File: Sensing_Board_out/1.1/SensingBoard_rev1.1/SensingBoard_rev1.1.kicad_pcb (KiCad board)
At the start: 2 copper layers, 40 x 40 mm, 52 parts, among them J1 USB_C_Receptacle, J2 3221-10-0300-00, J3 F32R-1A7H1-11024, J4 GRPB052VWQP-RC, J5 HMTSW-102-X-X-S-X, J6 HMTSW-102-X-X-S-X, J7 HMTSW-102-X-X-S-X, J8 HMTSW-102-X-X-S-X, SW1 PTS815 SJM 250 SMTR LFS, U1 ESP32C3, U2 BNO055, U3 MIC5504-3.3YM5, U4 FT232RQ

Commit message: finished power board
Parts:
- removed J8: HMTSW-102-X-X-S-X, HMTSW-102-X-X-S-X:SAMTEC_HMTSW-102-X-X-S-X
- added J9: RS1-02-G, RS1-02-G:CONN_RS1-02-G_ADM, F.Cu at (125.3, 41.9)
- J5, J6, J7: value HMTSW-102-X-X-S-X -> RS1-02-G; footprint HMTSW-102-X-X-S-X:SAMTEC_HMTSW-102-X-X-S-X -> RS1-02-G:CONN_RS1-02-G_ADM

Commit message: fixing POE board symbols + circuit
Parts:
- added C14: 1.6pF, Capacitor_SMD:C_0402_1005Metric, F.Cu at (96.5, 41.8)
- added C15: 1.6pF, Capacitor_SMD:C_0402_1005Metric, F.Cu at (96.5, 43.8)
- added C16: 18pF, Capacitor_SMD:C_0201_0603Metric, F.Cu at (99.2, 41.7)
- added C17: 18pF, Capacitor_SMD:C_0201_0603Metric, F.Cu at (99.2, 43.5)
- added C18: 100nF, Capacitor_SMD:C_0402_1005Metric, F.Cu at (96.5, 45.8)
- added C19: 10uF, Capacitor_SMD:C_0603_1608Metric, F.Cu at (107.3, 42.1)
- added C20: 1uF, Capacitor_SMD:C_0201_0603Metric, F.Cu at (99.2, 45.2)
- added C21: 10uF, Capacitor_SMD:C_0603_1608Metric, F.Cu at (107.3, 44.6)
- added C22: 1uF, Capacitor_SMD:C_0201_0603Metric, F.Cu at (99.2, 47.0)
- added C23: 10uF, Capacitor_SMD:C_0603_1608Metric, F.Cu at (107.3, 47.1)
- added C24: 1uF, Capacitor_SMD:C_0201_0603Metric, F.Cu at (101.6, 41.7)
- added C25: 10uF, Capacitor_SMD:C_0603_1608Metric, F.Cu at (107.3, 49.6)
- added C26: 1uF, Capacitor_SMD:C_0201_0603Metric, F.Cu at (101.6, 43.5)
- added C27: 2.2uF, Capacitor_SMD:C_0402_1005Metric, F.Cu at (96.5, 47.7)
- added C28: 2.2uF, Capacitor_SMD:C_0402_1005Metric, F.Cu at (96.5, 49.7)
- added C29: 100nF, Capacitor_SMD:C_0402_1005Metric, F.Cu at (96.5, 51.7)
- added D4: B140-E3, Diode_SMD:D_SMA, F.Cu at (107.9, 36.5)
- added FB1: 120R-3A, Capacitor_SMD:C_0805_2012Metric, F.Cu at (111.5, 51.3)
- added L1: 2nH, Inductor_SMD:L_01005_0402Metric, F.Cu at (113.1, 35.0)
- added L2: 2nH, Inductor_SMD:L_01005_0402Metric, F.Cu at (113.1, 36.7)
- added R21: 10k, Resistor_SMD:R_0201_0603Metric, F.Cu at (101.6, 45.2)
- added R22: 10k, Resistor_SMD:R_0201_0603Metric, F.Cu at (101.6, 47.0)
- added R23: 10k, Resistor_SMD:R_0201_0603Metric, F.Cu at (104.1, 41.7)
- added R24: 10k, Resistor_SMD:R_0201_0603Metric, F.Cu at (104.1, 43.5)
- added R25: 10k, Resistor_SMD:R_0201_0603Metric, F.Cu at (104.1, 45.2)
- added SW2: PTS815 SJM 250 SMTR LFS, PTS815:SW4_PTS815 SJM 250 SMTR LFS_CNK, F.Cu at (100.3, 38.3)
- added U5: MIC5504-1.8YM5, Package_TO_SOT_SMD:SOT-23-5, F.Cu at (111.9, 43.1)
- added U6: MCP1700x-280xxTT, Package_TO_SOT_SMD:SOT-23, F.Cu at (111.7, 47.5)
- added Y1: ABM8G-40.000MHZ-18-D2Y-T, ABM8G_40_000MHZ_18_D2Y_T:CRYSTAL_ABM8G_ABR, F.Cu at (101.8, 50.7)
- moved U4 35.8 mm to (121.4, 70.8)
- moved U1 1.17 mm to (129.0, 70.9)
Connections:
- ANT1 pad GND1: unconnected-(ANT1-PadGND1) -> GND
- ANT1 pad GND2: unconnected-(ANT1-PadGND2) -> GND
- ANT1 pad SIG: unconnected-(ANT1-PadSIG) -> Net-(ANT1-PadSIG)
- C1 pad 1: unconnected-(C1-Pad1) -> GND
- C2 pad 2: unconnected-(C2-Pad2) -> GND
- J3 pad 10: unconnected-(J3-Pad10) -> +1V8
- J3 pad 11: unconnected-(J3-Pad11) -> +2V8
- J3 pad 12: unconnected-(J3-Pad12) -> IO48/DVP_Y9
- J3 pad 13: unconnected-(J3-Pad13) -> IO10/XMCLK
- J3 pad 14: unconnected-(J3-Pad14) -> IO11/DVP_Y8
- J3 pad 15: unconnected-(J3-Pad15) -> GND
- J3 pad 16: unconnected-(J3-Pad16) -> IO12/DVP_Y7
- J3 pad 17: unconnected-(J3-Pad17) -> IO13/DVP_PCLK
- J3 pad 18: unconnected-(J3-Pad18) -> IO14/DVP_Y6
- J3 pad 19: unconnected-(J3-Pad19) -> IO15/DVP_Y2
- J3 pad 2: unconnected-(J3-Pad2) -> GND
- J3 pad 20: unconnected-(J3-Pad20) -> IO16/DVP_Y5
- J3 pad 21: unconnected-(J3-Pad21) -> IO17/DVP_Y3
- J3 pad 22: unconnected-(J3-Pad22) -> IO18/DVP_Y4
- J3 pad 23: unconnected-(J3-Pad23) -> GND
- J3 pad 24: unconnected-(J3-Pad24) -> Net-(D4-K)
- J3 pad 3: unconnected-(J3-Pad3) -> IO40/CAM_SDA
- J3 pad 4: unconnected-(J3-Pad4) -> Net-(FB1-Pad2)
- J3 pad 5: unconnected-(J3-Pad5) -> IO39/CAM_SCL
- J3 pad 6: unconnected-(J3-Pad6) -> CAM_RESET
- J3 pad 7: unconnected-(J3-Pad7) -> IO38/DVP_VSYNC
- J3 pad 8: unconnected-(J3-Pad8) -> Net-(J3-Pad8)
- J3 pad 9: unconnected-(J3-Pad9) -> IO47/DVP_HREF
- SW1 pad 1: unconnected-(SW1-Pad1) -> CHIP_EN
- U1 pad 1: unconnected-(U1-LNA_IN-Pad1) -> Net-(U1-LNA_IN)
- U1 pad 11: unconnected-(U1-VDD3P3_RTC-Pad11) -> VDD3P3_RTC
- U1 pad 17: unconnected-(U1-VDD3P3_CPU-Pad17) -> +3.3V
- U1 pad 18: unconnected-(U1-VDD_SPI-Pad18) -> VDD_SPI
- U1 pad 19: unconnected-(U1-SPIHD-Pad19) -> SPIHD
- U1 pad 2: +3.3V -> Net-(C18-Pad1)
- U1 pad 20: unconnected-(U1-SPIWP-Pad20) -> SPIWP
- U1 pad 21: unconnected-(U1-SPICS0-Pad21) -> SPICS0
- U1 pad 22: unconnected-(U1-SPICLK-Pad22) -> SPICLK
- U1 pad 23: unconnected-(U1-SPID-Pad23) -> SPID
- U1 pad 24: unconnected-(U1-SPIQ-Pad24) -> SPIQ
- U1 pad 29: unconnected-(U1-XTAL_N-Pad29) -> Net-(U1-XTAL_N)
- U1 pad 3: +3.3V -> Net-(C18-Pad1)
- U1 pad 30: unconnected-(U1-XTAL_P-Pad30) -> Net-(U1-XTAL_P)
- U1 pad 31: Net-(U1-VDDA-Pad31) -> +3.3V
- U1 pad 32: Net-(U1-VDDA-Pad31) -> +3.3V
- U1 pad 7: unconnected-(U1-CHIP_EN-Pad7) -> CHIP_EN

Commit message: sense board
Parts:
- added U7: ESP32-S3, ESP32S3:QFN56_7X7_EXP, F.Cu at (93.1, 65.0)

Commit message: completed sense board
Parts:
- removed C4: 22pF, Capacitor_SMD:C_0201_0603Metric
- removed D1: LED, LED_SMD:LED_0603_1608Metric
- removed J4: GRPB052VWQP-RC, GRPB052VWQP-RC:GRPB052VWQPRC
- removed R2: 100, Resistor_SMD:R_0201_0603Metric
- removed U1: ESP32C3, ESP32C3:QFN32_5X5MM
- removed XTAL1: ABS07-32.768KHZ-7-T, ABS07-32.768KHZ-7-T:XTAL_ABS07-32.768KHZ-7-T_ABR
- added C30: 100nF, Capacitor_SMD:C_0402_1005Metric, F.Cu at (166.9, 43.8)
- added C31: 2.2uF, Capacitor_SMD:C_0402_1005Metric, F.Cu at (166.9, 45.7)
- added C32: 2.2uF, Capacitor_SMD:C_0402_1005Metric, F.Cu at (166.9, 47.7)
- added C33: 2.2uF, Capacitor_SMD:C_0402_1005Metric, F.Cu at (166.9, 49.7)
- added C34: 100nF, Capacitor_SMD:C_0402_1005Metric, F.Cu at (166.9, 51.6)
- added C35: 10nF, Capacitor_SMD:C_0402_1005Metric, F.Cu at (166.9, 53.6)
- added C36: 100nF, Capacitor_SMD:C_0402_1005Metric, F.Cu at (166.9, 55.6)
- added C37: 100nF, Capacitor_SMD:C_0402_1005Metric, F.Cu at (166.9, 57.6)
- added R26: 499, Resistor_SMD:R_0201_0603Metric, F.Cu at (169.5, 43.7)
- added R27: 0k, Resistor_SMD:R_0201_0603Metric, F.Cu at (169.5, 45.4)
- added R28: 4.7k, Resistor_SMD:R_0201_0603Metric, F.Cu at (169.5, 47.2)
- C1: value 10uF -> 100nF; footprint Capacitor_SMD:C_0603_1608Metric -> Capacitor_SMD:C_0402_1005Metric
- C2: value 1uF -> 100nF; footprint Capacitor_SMD:C_0201_0603Metric -> Capacitor_SMD:C_0402_1005Metric
- C3: value 22pF -> 4.7uF; footprint Capacitor_SMD:C_0201_0603Metric -> Capacitor_SMD:C_0402_1005Metric
- R22: value 10k -> 0k
- R23: value 10k -> 4.7k
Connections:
- C1 pad 1: GND -> CAM_RESET
- C1 pad 2: +3.3V -> GND
- C14 pad 1: Net-(U1-LNA_IN) -> Net-(U7-LNA_IN)
- C16 pad 1: Net-(U1-XTAL_P) -> Net-(U7-XTAL_P)
- C17 pad 1: Net-(U1-XTAL_N) -> Net-(U7-XTAL_N)
- C3 pad 1: Net-(U1-XTAL_32K_P) -> +3.3V
- D2 pad 1: unconnected-(D2-K-Pad1) -> IO21/USER_LED
- D2 pad 2: unconnected-(D2-A-Pad2) -> Net-(D2-A)
- J3 pad 3: IO40/CAM_SDA -> MTDO/IO40/CAM_SDA
- J3 pad 5: IO39/CAM_SCL -> MTCK/IO39/CAM_SCL
- L1 pad 1: Net-(U1-LNA_IN) -> Net-(U7-LNA_IN)
- R1 pad 1: unconnected-(R1-Pad1) -> Net-(D2-A)
- R1 pad 2: unconnected-(R1-Pad2) -> +3.3V
- R10 pad 2: unconnected-(R10-Pad2) -> D3/A3
- R14 pad 2: unconnected-(R14-Pad2) -> GPIO35
- R15 pad 2: unconnected-(R15-Pad2) -> D2/A2
- R16 pad 2: unconnected-(R16-Pad2) -> D1/A1
- R17 pad 2: unconnected-(R17-Pad2) -> D0/A0
- R18 pad 2: unconnected-(R18-Pad2) -> GPIO37
- R19 pad 2: unconnected-(R19-Pad2) -> GPIO34
- R20 pad 2: unconnected-(R20-Pad2) -> GPIO33
- R22 pad 1: +2V8 -> Net-(R22-Pad1)
- R22 pad 2: IO40/CAM_SDA -> +2V8
- R23 pad 1: +2V8 -> Net-(R22-Pad1)
- R23 pad 2: IO39/CAM_SCL -> MTDO/IO40/CAM_SDA
- R9 pad 2: unconnected-(R9-Pad2) -> GPIO36
- SW2 pad 1: D9 -> GPIO0
- U7 pad 1: unconnected-(U7-LNA_IN-Pad1) -> Net-(U7-LNA_IN)
- U7 pad 10: unconnected-(U7-GPIO5-Pad10) -> D4/I2C_SDA
- U7 pad 11: unconnected-(U7-GPIO6-Pad11) -> D5/I2C_SCL
- U7 pad 12: unconnected-(U7-GPIO7-Pad12) -> D8/A8/SCK
- U7 pad 13: unconnected-(U7-GPIO8-Pad13) -> D9/A9/MISO
- U7 pad 14: unconnected-(U7-GPIO9-Pad14) -> D10/A10/MOSI
- U7 pad 15: unconnected-(U7-GPIO10-Pad15) -> IO10/XMCLK
- U7 pad 16: unconnected-(U7-GPIO11-Pad16) -> IO11/DVP_Y8
- U7 pad 17: unconnected-(U7-GPIO12-Pad17) -> IO12/DVP_Y7
- U7 pad 18: unconnected-(U7-GPIO13-Pad18) -> IO13/DVP_PCLK
- U7 pad 19: unconnected-(U7-GPIO14-Pad19) -> IO14/DVP_Y6
- U7 pad 2: unconnected-(U7-VDD3P3-Pad2) -> Net-(C18-Pad1)
- U7 pad 20: unconnected-(U7-VDD3P3_RTC-Pad20) -> +3.3V
- U7 pad 21: unconnected-(U7-XTAL_32K_P-Pad21) -> IO15/DVP_Y2
- U7 pad 22: unconnected-(U7-XTAL_32K_N-Pad22) -> IO16/DVP_Y5
- U7 pad 23: unconnected-(U7-GPIO17-Pad23) -> IO17/DVP_Y3
- U7 pad 24: unconnected-(U7-GPIO18-Pad24) -> IO18/DVP_Y4
- U7 pad 25: unconnected-(U7-GPIO19-Pad25) -> USB_DN
- U7 pad 26: unconnected-(U7-GPIO20-Pad26) -> USB_DP
- U7 pad 27: unconnected-(U7-GPIO21-Pad27) -> IO21/USER_LED
- U7 pad 29: unconnected-(U7-VDD_SPI-Pad29) -> VDD_SPI
- U7 pad 3: unconnected-(U7-VDD3P3-Pad3) -> Net-(C18-Pad1)
- U7 pad 30: unconnected-(U7-SPIHD-Pad30) -> SPIHD
- U7 pad 31: unconnected-(U7-SPIWP-Pad31) -> SPIWP
- U7 pad 32: unconnected-(U7-SPICS0-Pad32) -> SPICS0
- U7 pad 33: unconnected-(U7-SPICLK-Pad33) -> SPICLK
- U7 pad 34: unconnected-(U7-SPIQ-Pad34) -> SPIQ
- U7 pad 35: unconnected-(U7-SPID-Pad35) -> SPID
- U7 pad 36: unconnected-(U7-SPICLK_N-Pad36) -> IO48/DVP_Y9
- U7 pad 37: unconnected-(U7-SPICLK_P-Pad37) -> IO47/DVP_HREF
- U7 pad 38: unconnected-(U7-GPIO33-Pad38) -> GPIO33
- U7 pad 39: unconnected-(U7-GPIO34-Pad39) -> GPIO34
- U7 pad 4: unconnected-(U7-CHIP_PU-Pad4) -> CHIP_EN
- U7 pad 40: unconnected-(U7-GPIO35-Pad40) -> GPIO35
- U7 pad 41: unconnected-(U7-GPIO36-Pad41) -> GPIO36
- U7 pad 42: unconnected-(U7-GPIO37-Pad42) -> GPIO37
- U7 pad 43: unconnected-(U7-GPIO38-Pad43) -> IO38/DVP_VSYNC
- U7 pad 44: unconnected-(U7-MTCK-Pad44) -> MTCK/IO39/CAM_SCL
- U7 pad 45: unconnected-(U7-MTDO-Pad45) -> MTDO/IO40/CAM_SDA
- U7 pad 46: unconnected-(U7-VDD3P3_CPU-Pad46) -> +3.3V
- U7 pad 47: unconnected-(U7-MTDI-Pad47) -> MTDI/IO41/PDM_DATA
- U7 pad 48: unconnected-(U7-MTMS-Pad48) -> MTMS/IO42/PDM_CLK
- U7 pad 49: unconnected-(U7-U0TXD-Pad49) -> Net-(U7-U0TXD)
- U7 pad 5: unconnected-(U7-GPIO0-Pad5) -> GPIO0
- U7 pad 50: unconnected-(U7-U0RXD-Pad50) -> RX_D7
- U7 pad 53: unconnected-(U7-XTAL_N-Pad53) -> Net-(U7-XTAL_N)
- U7 pad 54: unconnected-(U7-XTAL_P-Pad54) -> Net-(U7-XTAL_P)
- U7 pad 55: unconnected-(U7-VDDA-Pad55) -> +3.3V
- U7 pad 56: unconnected-(U7-VDDA-Pad56) -> +3.3V
- U7 pad 57: unconnected-(U7-GND-Pad57) -> GND
- U7 pad 6: unconnected-(U7-GPIO1-Pad6) -> D0/A0
- U7 pad 7: unconnected-(U7-GPIO2-Pad7) -> D1/A1
- U7 pad 8: unconnected-(U7-GPIO3-Pad8) -> D2/A2
- U7 pad 9: unconnected-(U7-GPIO4-Pad9) -> D3/A3
- Y1 pad 1: Net-(U1-XTAL_N) -> Net-(U7-XTAL_N)
- Y1 pad 3: Net-(U1-XTAL_P) -> Net-(U7-XTAL_P)

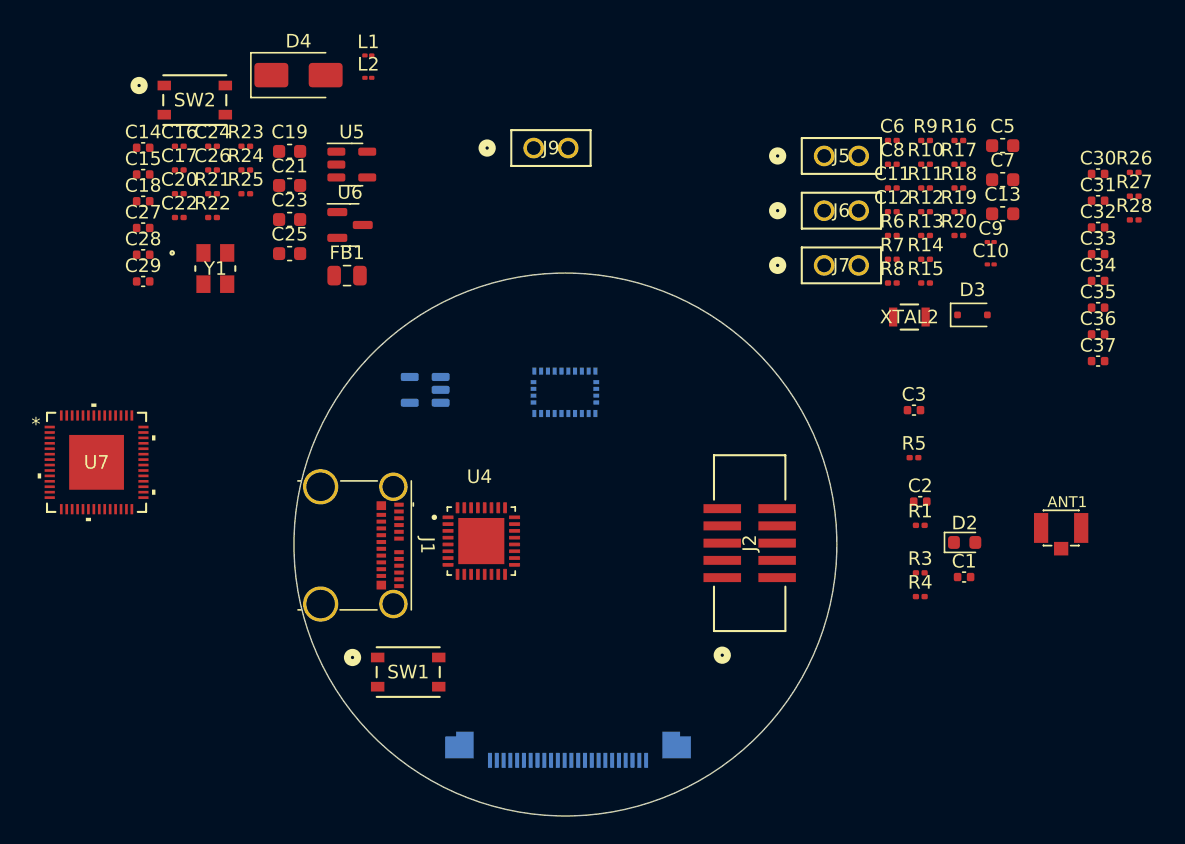
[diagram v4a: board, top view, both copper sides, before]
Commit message: updated power
finished swapping power board bulk cap, new POE board schematic
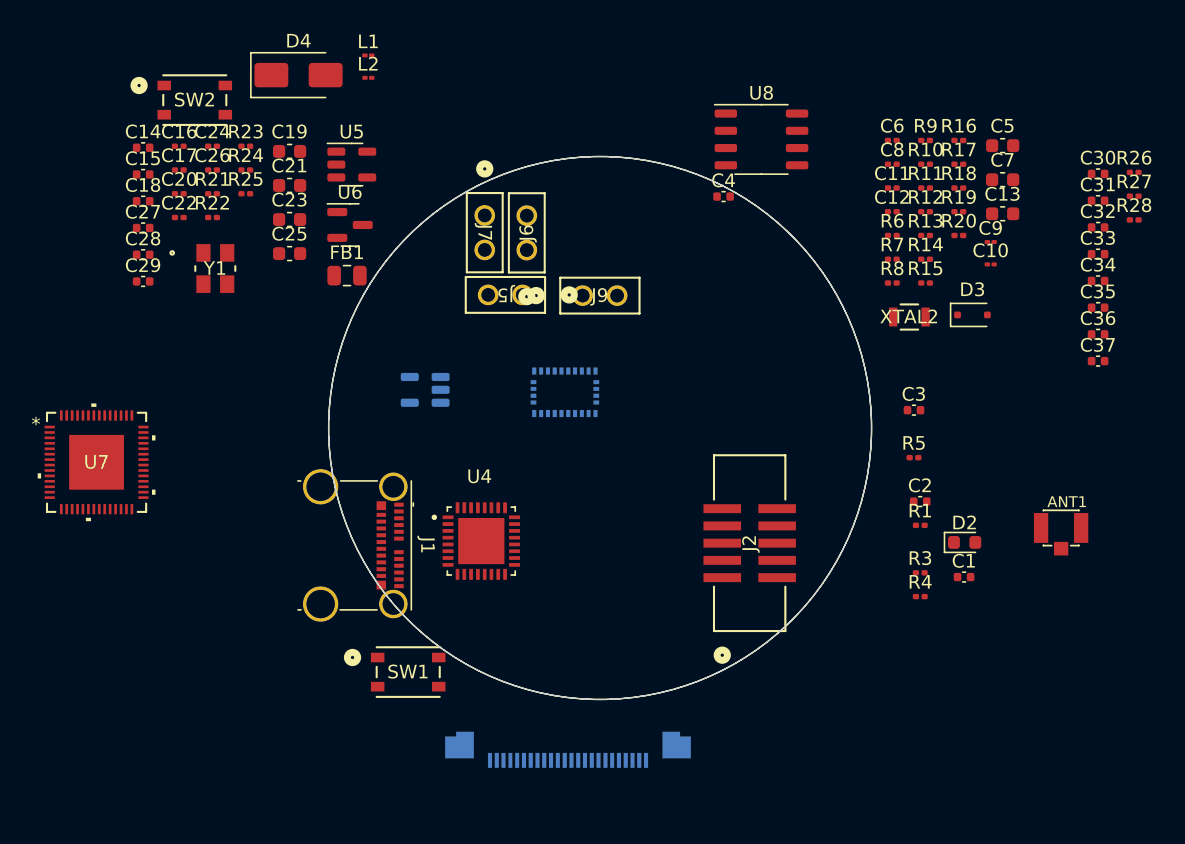
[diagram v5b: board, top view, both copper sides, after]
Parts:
- added C4: 100nF, Capacitor_SMD:C_0402_1005Metric, F.Cu at (139.3, 45.4)
- added U8: GD25D05CT, Package_SO:SOP-8_3.9x4.9mm_P1.27mm, F.Cu at (142.1, 41.2)
- moved J7 25.3 mm to (121.7, 46.8), turned to -90 degrees
- moved J5 24.5 mm to (124.5, 52.7), turned to 180 degrees
- moved J6 22.1 mm to (124.8, 49.4), turned to 90 degrees
- moved J9 11.5 mm to (128.9, 52.7)

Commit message: sense board layout
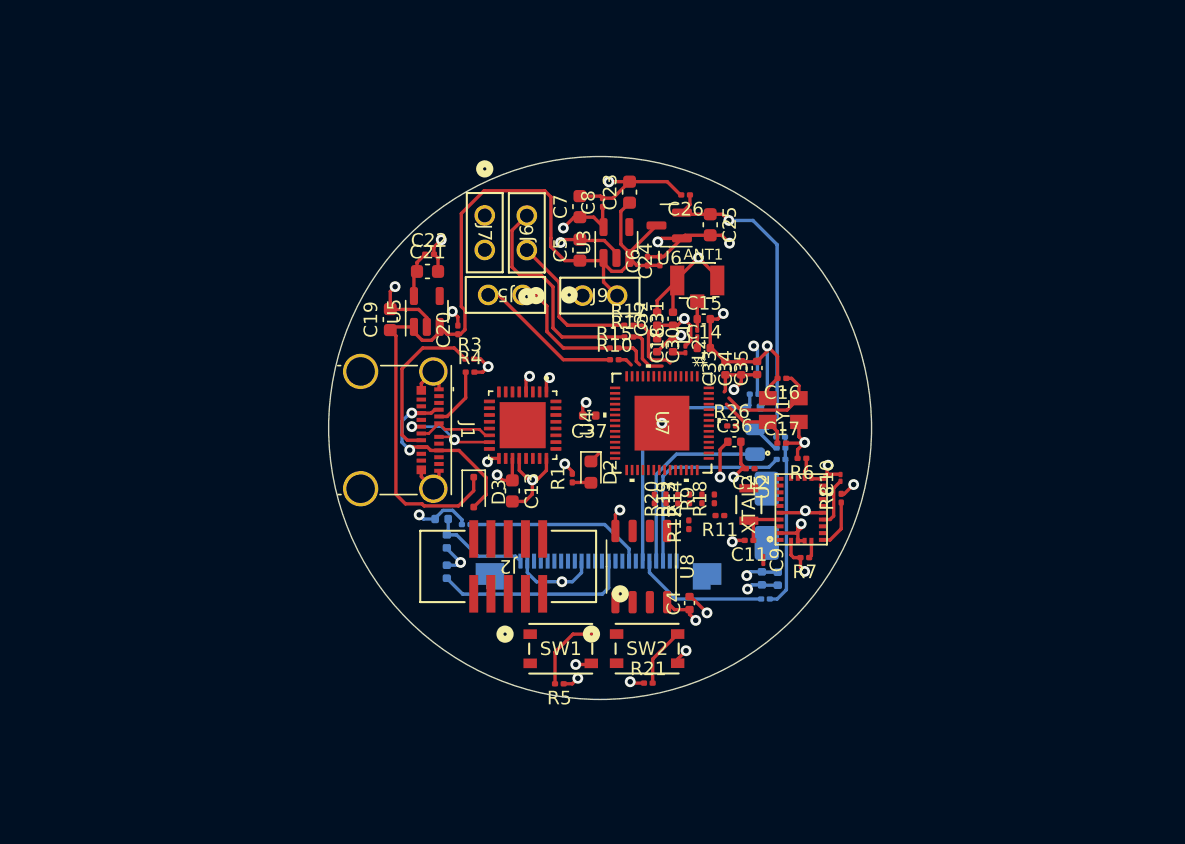
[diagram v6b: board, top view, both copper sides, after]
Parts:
- C1, C2, C27, C28, C29, C3, D4, FB1, R22, R23, R24, R25, R27, R28: moved to B.Cu
- U2, U3: moved to F.Cu
- moved SW2 52.4 mm to (133.6, 78.7)
- moved C17 48.7 mm to (143.5, 63.6)
- moved R21 48.3 mm to (133.7, 81.3)
- moved C16 47.6 mm to (143.6, 58.8), turned to 180 degrees
- moved D4 47.4 mm to (142.4, 69.0), turned to 90 degrees
- moved R23 45.7 mm to (143.5, 64.8), turned to 180 degrees
- moved R22 45.2 mm to (143.5, 64.0), turned to 180 degrees
- moved C14 43.9 mm to (137.8, 56.6)
- moved Y1 43.1 mm to (143.7, 61.2), turned to 90 degrees
- moved C15 42.7 mm to (137.8, 54.5)
- moved U7 41.8 mm to (134.7, 62.1), turned to -90 degrees
- moved C13 41.5 mm to (123.7, 67.1), turned to -90 degrees
- moved R24 40.9 mm to (141.5, 60.0), turned to 180 degrees
- moved C18 40.4 mm to (135.5, 56.4), turned to 90 degrees
- moved D3 39.0 mm to (120.9, 67.2), turned to -90 degrees
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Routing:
- net GND: track 0.00 -> 123.2 mm, vias 0 -> 32
- net VDC: track 0.00 -> 67.9 mm
- net +2V8: track 0.00 -> 41.1 mm, vias 0 -> 1
- net +3.3V: track 0.00 -> 38.7 mm, vias 0 -> 13
- net CAM_RESET: track 0.00 -> 19.4 mm
- net MOTOR2_BIN1: track 0.00 -> 16.4 mm
- net MTDO/IO40/CAM_SDA: track 0.00 -> 15.1 mm
- net +5V: track 0.00 -> 14.7 mm, vias 0 -> 2
- net Net-(FB1-Pad2): track 0.00 -> 14.3 mm
- net Net-(J3-Pad8): track 0.00 -> 13.3 mm
- net Net-(R22-Pad1): track 0.00 -> 12.8 mm
- net Net-(J1-CC2): track 0.00 -> 12.1 mm
- net MOTOR2_BIN2: track 0.00 -> 11.0 mm
- net MOTOR1_AIN1: track 0.00 -> 11.0 mm
- net MTCK/IO39/CAM_SCL: track 0.00 -> 9.89 mm
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- added copper zone on In2.Cu, net +3.3V
- added copper zone on In1.Cu, net GND
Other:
- copper layers 2 -> 4
